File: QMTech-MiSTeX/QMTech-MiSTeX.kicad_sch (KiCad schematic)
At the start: 42 parts, among them J1 RPi_GPIO, J12 Conn_01x03_Pin, J13 USB_C_Receptacle_USB2.0, J2 MiSTer SDRAM Module, J3 USB_C_Receptacle_USB2.0, J4 Conn_02x32_Odd_Even, J5 Conn_02x32_Odd_Even, J6 Conn_01x06_Pin, J7 Conn_01x03_Pin, J8 Conn_01x03_Pin

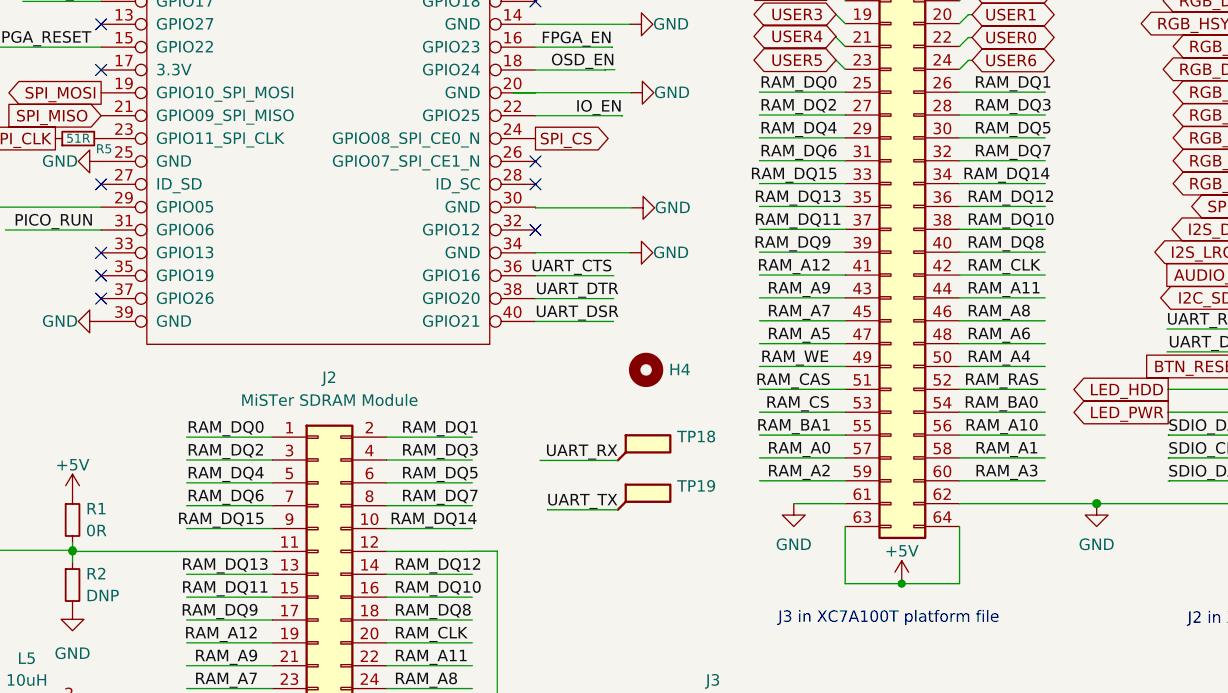
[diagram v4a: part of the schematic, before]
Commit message: QMTech-MiSTeX: fix swapped DQ14/15 pins
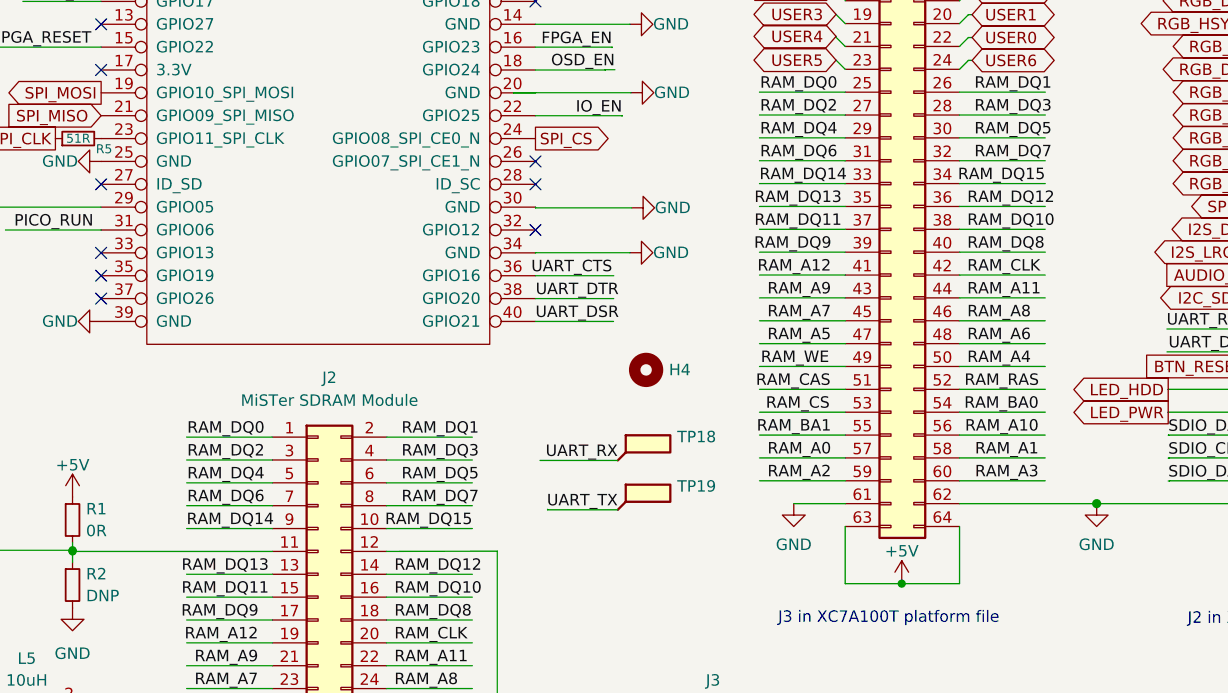
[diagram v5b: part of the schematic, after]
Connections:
- net RAM_DQ14: now also J2.9 (Pin_9), J4.33 (Pin_33); no longer J2.10 (Pin_10), J4.34 (Pin_34)
- net RAM_DQ15: now also J2.10 (Pin_10), J4.34 (Pin_34); no longer J2.9 (Pin_9), J4.33 (Pin_33)
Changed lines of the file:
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@@
     (effects (font (size 1.27 1.27)) (justify right bottom))
   )
-  (label "RAM_DQ14" (at 136.6563 59.6646 0) (fields_autoplaced)
+  (label "RAM_DQ14" (at 114.046 59.6646 0) (fields_autoplaced)
     (effects (font (size 1.27 1.27)) (justify left bottom))
   )
@@
     (effects (font (size 1.27 1.27)) (justify right bottom))
   )
-  (label "RAM_DQ14" (at 73.0039 97.9932 0) (fields_autoplaced)
+  (label "RAM_DQ14" (at 50.3936 97.9932 0) (fields_autoplaced)
     (effects (font (size 1.27 1.27)) (justify left bottom))
   )
@@
     (effects (font (size 1.27 1.27)) (justify left bottom))
   )
-  (label "RAM_DQ15" (at 59.0883 97.9932 180) (fields_autoplaced)
+  (label "RAM_DQ15" (at 82.1436 97.9932 180) (fields_autoplaced)
     (effects (font (size 1.27 1.27)) (justify right bottom))
   )
@@
     (effects (font (size 1.27 1.27)) (justify right bottom))
   )
-  (label "RAM_DQ15" (at 122.7407 59.6646 180) (fields_autoplaced)
+  (label "RAM_DQ15" (at 145.796 59.6646 180) (fields_autoplaced)
     (effects (font (size 1.27 1.27)) (justify right bottom))
   )

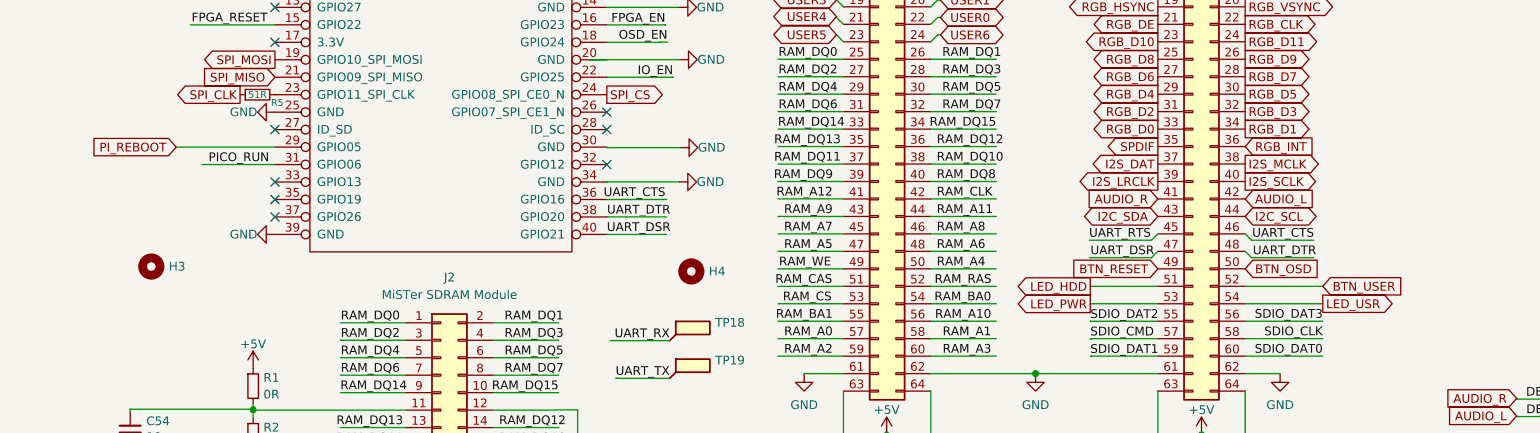
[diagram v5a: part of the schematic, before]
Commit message: connect buttons to the HPS, not the FPGA, because the FPGA does not use them
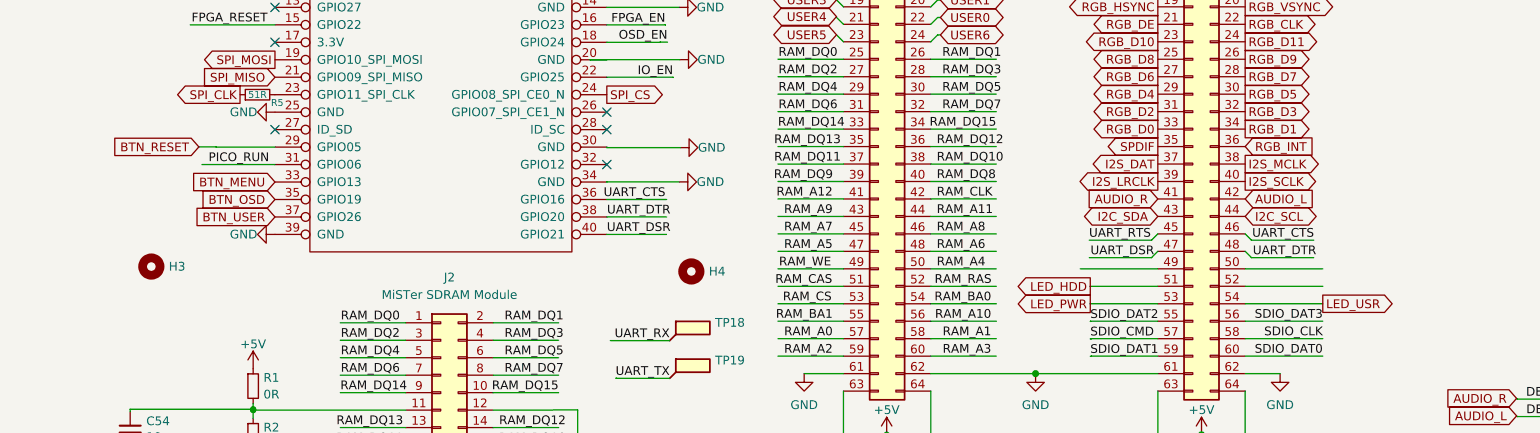
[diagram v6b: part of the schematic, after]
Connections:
- net PI_REBOOT is gone; now on net BTN_RESET: J1.29 (GPIO05)
- net BTN_OSD: now also J1.35 (GPIO19); no longer J5.50 (Pin_50)
- net BTN_RESET: no longer J5.49 (Pin_49)
- net BTN_USER: now also J1.37 (GPIO26); no longer J5.52 (Pin_52)
- net BTN_MENU: now reaches J1.33 (GPIO13)
- no-connect marks 23 -> 20
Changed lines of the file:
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@@
   (no_connect (at 89.154 64.8208))
   (no_connect (at 89.154 59.7408))
-  (no_connect (at 40.894 67.3608))
   (no_connect (at 89.154 39.4208))
   (no_connect (at 40.894 47.0408))
@@
   (no_connect (at 84.7598 167.1066))
   (no_connect (at 121.412 121.6406))
-  (no_connect (at 40.894 72.4408))
-  (no_connect (at 40.894 69.9008))
   (no_connect (at 121.412 149.5806))
   (no_connect (at 84.7598 162.0266))
@@
     (stroke (width 0) (type default))
   )
+  (wire (pts (xy 169.291 79.9846) (xy 158.0038 79.9846))
+    (stroke (width 0) (type default))
+  )
   (wire (pts (xy 59.9186 105.6132) (xy 50.3936 105.6132))
     (stroke (width 0) (type default))
@@
     (stroke (width 0) (type default))
   )
+  (wire (pts (xy 193.2782 79.9846) (xy 181.991 79.9846))
+    (stroke (width 0) (type default))
+  )
   (wire (pts (xy 37.719 100.4062) (xy 37.719 99.5819))
     (stroke (width 0) (type default))
@@
     (stroke (width 0) (type default))
   )
-  (wire (pts (xy 26.5302 62.2808) (xy 40.894 62.2808))
+  (wire (pts (xy 29.8237 62.2518) (xy 32.3637 62.2518))
     (stroke (width 0) (type default))
   )
@@
     (stroke (width 0) (type default))
   )
+  (wire (pts (xy 32.3637 62.2518) (xy 32.3637 62.2808))
+    (stroke (width 0) (type default))
+  )
   (wire (pts (xy 97.9763 47.0144) (xy 96.9184 47.0144))
     (stroke (width 0) (type default))
@@
     (stroke (width 0) (type default))
   )
+  (wire (pts (xy 32.3637 62.2808) (xy 40.894 62.2808))
+    (stroke (width 0) (type default))
+  )
   (wire (pts (xy 208.7626 132.3848) (xy 208.7626 132.1308))
     (stroke (width 0) (type default))
@@
     (effects (font (size 1.27 1.27)) (justify right bottom))
   )
-  (global_label "BTN_OSD" (shape input) (at 181.991 79.9846 0) (fields_autoplaced)
-    (effects (font (size 1.27 1.27)) (justify left))
-    (property "Intersheetrefs" "${INTERSHEET_REFS}" (at 193.417 79.9846 0)
-      (effects (font (size 1.27 1.27)) (justify left))
+  (global_label "BTN_OSD" (shape input) (at 40.894 69.9008 180) (fields_autoplaced)
+    (effects (font (size 1.27 1.27)) (justify right))
+    (property "Intersheetrefs" "${INTERSHEET_REFS}" (at 29.468 69.9008 0)
+      (effects (font (size 1.27 1.27)) (justify right))
     )
   )
@@
     )
   )
-  (global_label "PI_REBOOT" (shape input) (at 26.5302 62.2808 180) (fields_autoplaced)
+  (global_label "BTN_MENU" (shape input) (at 40.894 67.3608 180) (fields_autoplaced)
     (effects (font (size 1.27 1.27)) (justify right))
-    (property "Intersheetrefs" "${INTERSHEET_REFS}" (at 13.385 62.2808 0)
+    (property "Intersheetrefs" "${INTERSHEET_REFS}" (at 28.0166 67.3608 0)
       (effects (font (size 1.27 1.27)) (justify right))
     )
@@
     )
   )
-  (global_label "BTN_RESET" (shape input) (at 169.291 79.9846 180) (fields_autoplaced)
+  (global_label "BTN_RESET" (shape input) (at 29.8237 62.2518 180) (fields_autoplaced)
     (effects (font (size 1.27 1.27)) (justify right))
-    (property "Intersheetrefs" "${INTERSHEET_REFS}" (at 156.025 79.9846 0)
+    (property "Intersheetrefs" "${INTERSHEET_REFS}" (at 16.5577 62.2518 0)
       (effects (font (size 1.27 1.27)) (justify right))
     )
@@
     )
   )
-  (global_label "BTN_USER" (shape input) (at 193.2782 82.5246 0) (fields_autoplaced)
-    (effects (font (size 1.27 1.27)) (justify left))
-    (property "Intersheetrefs" "${INTERSHEET_REFS}" (at 205.7581 82.5246 0)
-      (effects (font (size 1.27 1.27)) (justify left))
+  (global_label "BTN_USER" (shape input) (at 40.894 72.4408 180) (fields_autoplaced)
+    (effects (font (size 1.27 1.27)) (justify right))
+    (property "Intersheetrefs" "${INTERSHEET_REFS}" (at 28.319 72.4408 0)
+      (effects (font (size 1.27 1.27)) (justify right))
     )
   )

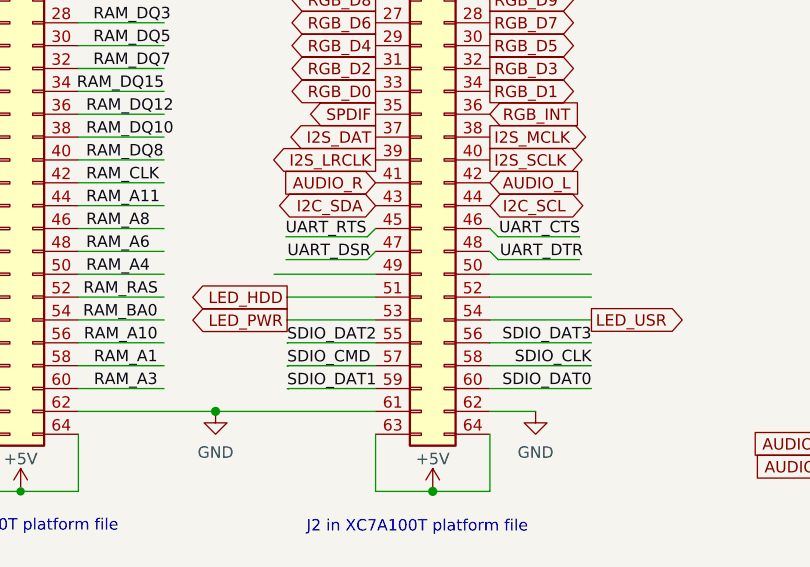
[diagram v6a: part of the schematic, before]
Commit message: use stricter design rules and cleanup all DRC errors
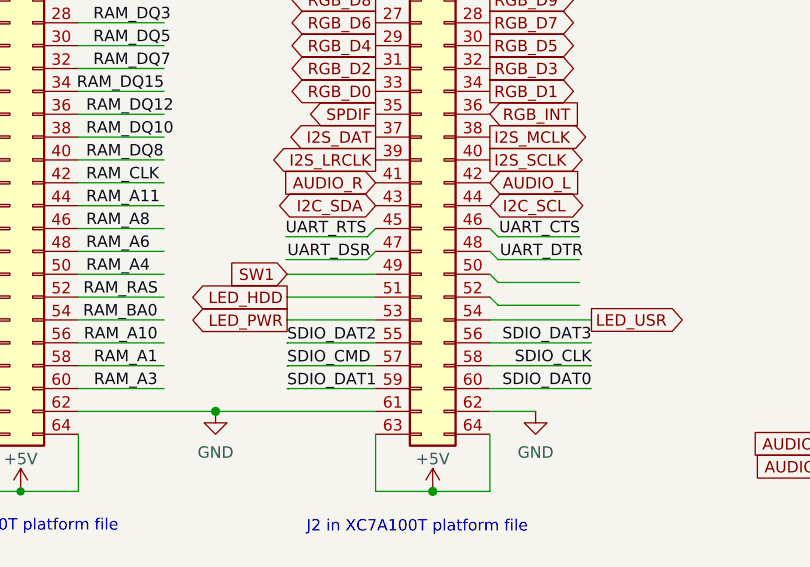
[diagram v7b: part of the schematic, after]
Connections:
- net SW1: now reaches J5.49 (Pin_49)
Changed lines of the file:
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@@
     (stroke (width 0) (type default))
   )
+  (wire (pts (xy 182.9054 80.899) (xy 181.991 79.9846))
+    (stroke (width 0) (type default))
+  )
   (wire (pts (xy 151.511 19.0246) (xy 169.291 19.0246))
     (stroke (width 0) (type solid))
@@
     (stroke (width 0) (type default))
   )
-  (wire (pts (xy 169.291 79.9846) (xy 158.0038 79.9846))
-    (stroke (width 0) (type default))
-  )
   (wire (pts (xy 59.9186 105.6132) (xy 50.3936 105.6132))
     (stroke (width 0) (type default))
@@
     (stroke (width 0) (type default))
   )
-  (wire (pts (xy 193.2782 82.5246) (xy 181.991 82.5246))
-    (stroke (width 0) (type default))
-  )
   (wire (pts (xy 84.8614 123.3678) (xy 84.8614 137.5664))
     (stroke (width 0) (type default))
@@
     (stroke (width 0) (type default))
   )
-  (wire (pts (xy 193.2782 79.9846) (xy 181.991 79.9846))
-    (stroke (width 0) (type default))
-  )
   (wire (pts (xy 37.719 100.4062) (xy 37.719 99.5819))
     (stroke (width 0) (type default))
@@
     (stroke (width 0) (type default))
   )
+  (wire (pts (xy 169.291 79.9846) (xy 159.4612 79.9846))
+    (stroke (width 0) (type default))
+  )
   (wire (pts (xy 191.9595 75.819) (xy 182.9054 75.819))
     (stroke (width 0) (type default))
@@
     (stroke (width 0) (type default))
   )
+  (wire (pts (xy 182.9054 83.439) (xy 181.991 82.5246))
+    (stroke (width 0) (type default))
+  )
   (wire (pts (xy 123.571 52.0446) (xy 114.046 52.0446))
     (stroke (width 0) (type default))
@@
     (stroke (width 0) (type default))
   )
+  (wire (pts (xy 191.9595 80.899) (xy 182.9054 80.899))
+    (stroke (width 0) (type default))
+  )
   (wire (pts (xy 193.2782 85.0646) (xy 181.991 85.0646))
     (stroke (width 0) (type default))
@@
     (stroke (width 0) (type default))
   )
+  (wire (pts (xy 191.9595 83.439) (xy 182.9054 83.439))
+    (stroke (width 0) (type default))
+  )
   (wire (pts (xy 23.5458 117.3619) (xy 23.5458 114.9096))
     (stroke (width 0) (type default))
@@
       (effects (font (size 1.27 1.27)) (justify right))
     )
+  )
+  (global_label "SW1" (shape input) (at 159.4612 79.9846 180) (fields_autoplaced)
+    (effects (font (size 1.27 1.27)) (justify right))
+    (property "Intersheetrefs" "${INTERSHEET_REFS}" (at 152.5105 79.9846 0)
+      (effects (font (size 1.27 1.27)) (justify right))
+    )
